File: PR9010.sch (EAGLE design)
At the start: 49 parts, among them U1 SI4703, U2 Tiny85-20-SMT, Y1 32.768kHz

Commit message: Schematics Updates
Recommendations from Andy
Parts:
- removed C15: 1nF, resistor:C-USC0603
- removed L2: 56nH, SparkFun-Passives:INDUCTOR0603
- removed MCU_IO: (no value), SparkFun-Connectors:M06LONGPADS
- removed U$1, U$2: BK-92_MPD_AA_BATT_CLIP, PR_Libraries:BK-92_MPD_AA_BATT_CLIP
- added C10, C13, C8: (no value), SparkFun-Capacitors:1.0UF-25V-+80/-20(0805)
- added J1: AVR_SPI_PRG_6NS, SparkFun-Connectors:AVR_SPI_PRG_6NS
- added L1: (no value), SparkFun-Passives:INDUCTOR0805
- added LED1: (no value), led:LEDSML0603
- added PWRIN, U1AOUT: M02PTH3, SparkFun-Connectors:M02PTH3
- C1: value 0.1uF -> (none); device SparkFun:CAP0402-CAP -> SparkFun-Capacitors:1.0UF-25V-+80/-20(0805)
- C2: value 22nF -> (none); device SparkFun:CAP0402-CAP -> SparkFun-Capacitors:1.0UF-25V-+80/-20(0805)
- C27: value 470pF -> (none)
- C6: value 2.2uF -> (none); device SparkFun:CAP0402-CAP -> SparkFun-Capacitors:1.0UF-25V-+80/-20(0805)
- R5: value 1k -> 1K; device SparkFun:RESISTOR0402-RES -> resistor:R-US_R0603
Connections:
- removed net N$29: C15.2, L2.1, U1.FMIP
- removed net N$30: U$1.NEG, U$2.POS
- removed net N$32: U$1.POS, U$5.SW_OUT
- new net N$10: C1.1, C13.1, C2.1, C6.1, L3.2
- new net N$6: C10.2, L1.1, U1.FMIP
- new net N$7: LED1.A, R5.1
- net 3.3V: now also U$5.SW_OUT; no longer C1.1, C2.1, L3.2, U1.VA, U1.VD, U1.VIO
- net A_IN: no longer C6.2
- net GND: now also C13.2, C6.2, C8.2, J1.6, L1.2, LED1.C, PWRIN.2; no longer L2.2, R19.1, U$2.NEG
- net N$18: now also R15.2
- net N$19: now also C10.1, C8.1; no longer C15.1
- net N$35: now also R19.1; no longer R19.2
- net N$9: now also U1.VA, U1.VD, U1.VIO; no longer R5.2, ST_CH.P1
- net OUT+: no longer AMP.OUT+
- net PB0: now also J1.4; no longer MCU_IO.6
- net PB1: now also J1.1; no longer MCU_IO.5
- net PB2: now also J1.3; no longer MCU_IO.4
- net PB3: now also ST_CH.P1, U1AOUT.1; no longer MCU_IO.3, R5.1
- net PB4: now also R5.2, U1AOUT.2; no longer MCU_IO.2
- net PB5: now also J1.5; no longer MCU_IO.1
- net ROUT: no longer C6.1, U1.ROUT
- net VCC: now also J1.2; no longer R15.2
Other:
- moved on the sheet: C1, C12, C2, C27, C5, C6, C7, ESD, L3, R1, R19, R5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

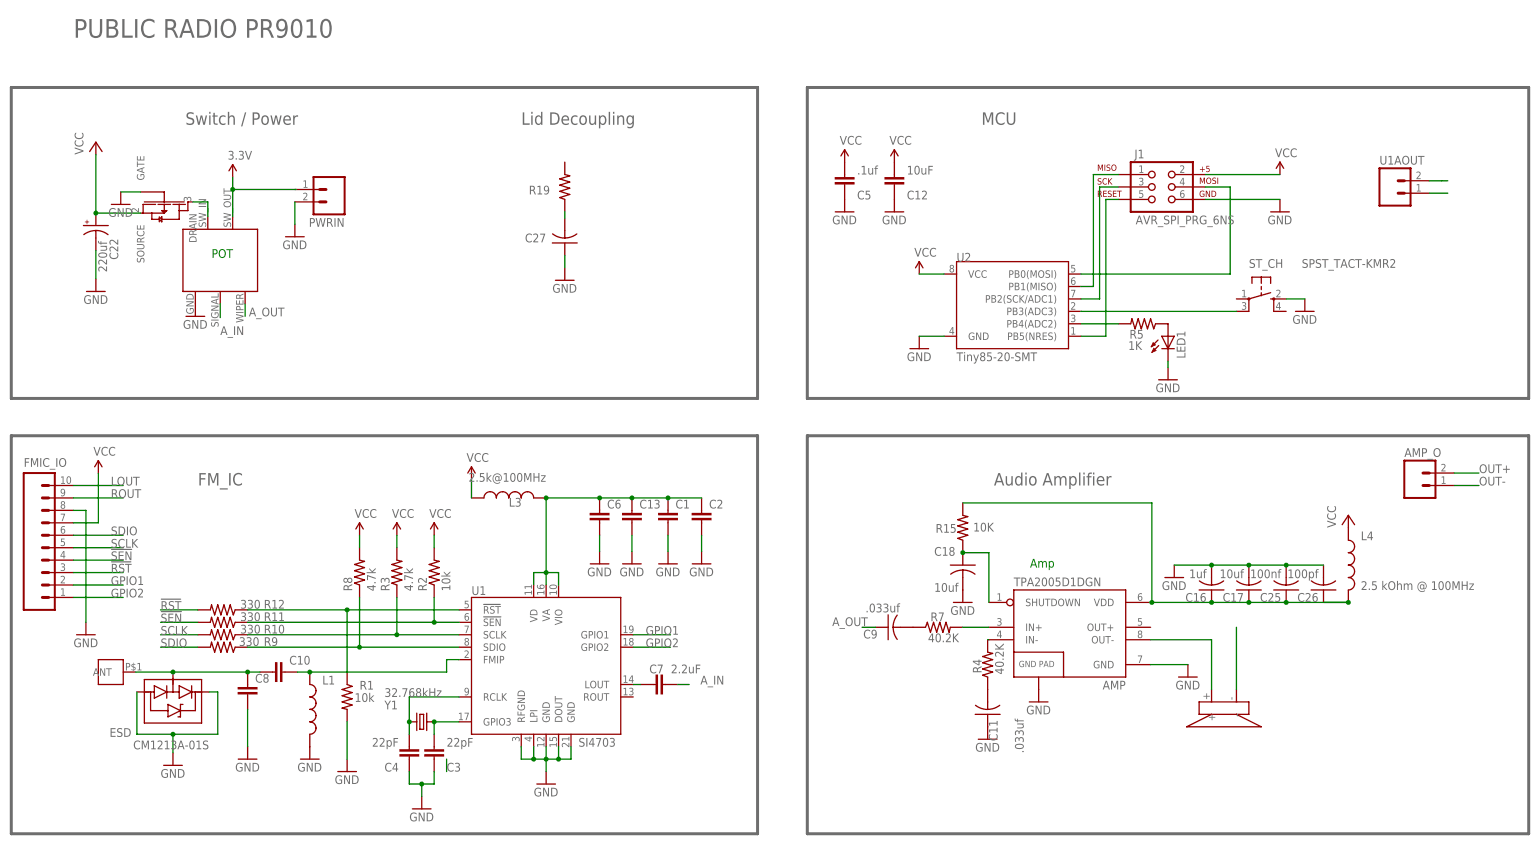
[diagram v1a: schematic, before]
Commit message: Sch Updates
Updates from Andy’s recommendations
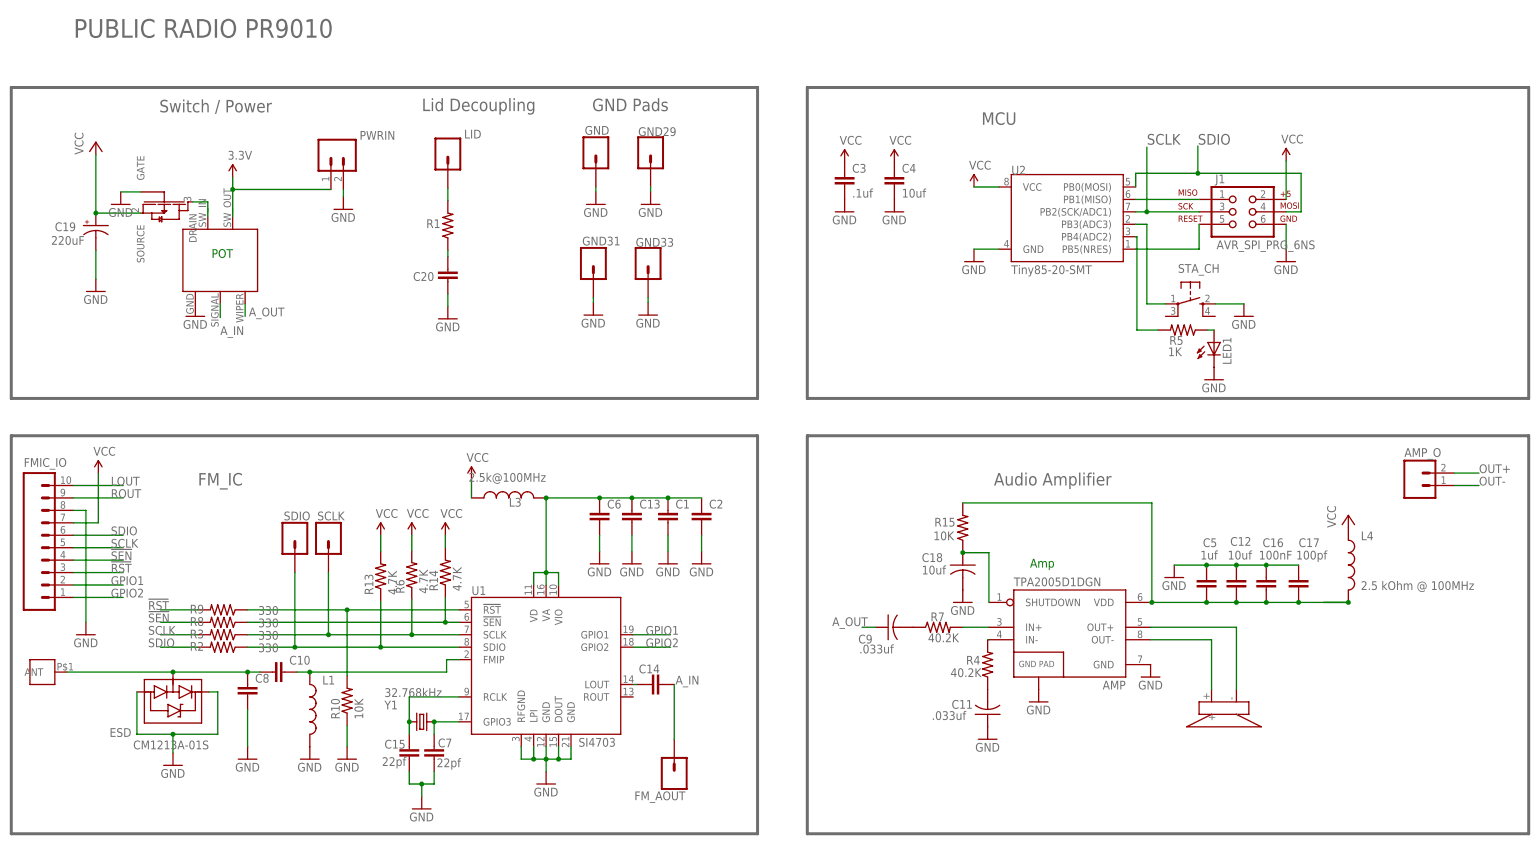
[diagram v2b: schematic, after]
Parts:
- removed C22: 220uf, CPOL-US-LongPads :CPOL-USE2-5
- removed C25: 100nf, resistor:C-USC0603
- removed C26: 100pf, resistor:C-USC0603
- removed C27: (no value), resistor:C-USC0603
- removed R11, R12: 330, SparkFun:RESISTOR0402-RES
- removed R19: 0Ohm, resistor:R-US_R0603
- removed ST_CH: SPST_TACT-KMR2, adafruit:SPST_TACT-KMR2
- removed U1AOUT: M02PTH3, SparkFun-Connectors:M02PTH3
- added C14: 4.7uF, SparkFun-Capacitors:1.0UF-25V-+80/-20(0805)
- added C15: 22pf, SparkFun-Passives:CAP0805
- added C19: 220uF, SparkFun-Passives:CAP_POLC
- added C20: (no value), SparkFun-Passives:CAP0805
- added FM_AOUT, GND, GND29, GND31, GND33, LID, SCLK, SDIO: M01PTH, SparkFun-Connectors:M01PTH
- added R13, R14, R6: 4.7K, SparkFun-Passives:RESISTOR0805-RES
- added STA_CH: SPST_TACT-KMR2, adafruit:SPST_TACT-KMR2
- C12: value 10uF -> 10uf; device SparkFun:CAP0402-CAP -> SparkFun-Passives:CAP0805
- C16: value 1uf -> 100nF; device resistor:C-USC0603 -> SparkFun-Passives:CAP0805
- C17: value 10uf -> 100pf; device resistor:C-USC0603 -> SparkFun-Passives:CAP0805
- C3: value 22pF -> .1uf; device SparkFun:CAP0402-CAP -> SparkFun-Passives:CAP0805
- C4: value 22pF -> 10uf; device SparkFun:CAP0402-CAP -> SparkFun-Passives:CAP0805
- C5: value .1uf -> 1uf; device SparkFun:CAP0402-CAP -> SparkFun-Passives:CAP0805
- C7: value 2.2uF -> 22pf; device SparkFun:CAP0402-CAP -> SparkFun-Passives:CAP0805
- R1: value 10k -> (none); device SparkFun:RESISTOR0402-RES -> SparkFun-Passives:RESISTOR0805-RES
- R10: value 330 -> 10K; device SparkFun:RESISTOR0402-RES -> SparkFun-Passives:RESISTOR0805-RES
- R2: value 10k -> 330; device SparkFun:RESISTOR0402-RES -> SparkFun-Passives:RESISTOR0805-RES
- R3, R8: value 4.7k -> 330; device SparkFun:RESISTOR0402-RES -> SparkFun-Passives:RESISTOR0805-RES
- R9: device SparkFun:RESISTOR0402-RES -> SparkFun-Passives:RESISTOR0805-RES
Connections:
- removed net PB0: J1.4, U2.PB0(MOSI)
- removed net PB2: J1.3, U2.PB2(SCK/ADC1)
- removed net PB3: ST_CH.P1, U1AOUT.1, U2.PB3(ADC3)
- removed net PB4: R5.2, U1AOUT.2, U2.PB4(ADC2)
- new net N$11: STA_CH.P, U2.PB3(ADC3)
- new net N$12: R5.2, U2.PB4(ADC2)
- new net N$8: LID.1, R1.2
- net !RST: now also R9.2; no longer R12.2
- net !RST-L: now also R10.2, R9.1; no longer R1.1, R12.1
- net !SEN: now also R8.2; no longer R11.2
- net !SEN-L: now also R14.1, R8.1; no longer R11.1, R2.1
- net 3.3V: now also PWRIN.1, R13.2, R14.2, R6.2; no longer R2.2, R3.2, R8.2
- net A_IN: now also C14.2, FM_AOUT.1; no longer C7.2
- net GND: now also C15.2, C16.1, C17.1, C19.-, C20.2, C3.2, C4.2, C7.2, GND.1, GND29.1, GND31.1, GND33.1, R10.1, STA_CH.S; no longer C16.2, C17.2, C22.-, C25.2, C26.2, C27.1, C3.1, C4.1, R1.2, ST_CH.S
- net LOUT: now also C14.1; no longer C7.1
- net N$1: now also C15.1; no longer C4.2
- net N$18: now also C12.2, C16.2, C17.2, C5.2; no longer C16.1, C17.1, C25.1, C26.1
- net N$2: now also C7.1; no longer C3.2
- net N$35: now also C20.1, R1.1; no longer C27.2, R19.1
- net OUT+: now also AMP.OUT+
- net SCLK: now also J1.3, R3.2, U2.PB2(SCK/ADC1); no longer R10.2
- net SCLK-L: now also R6.1, SCLK.1; no longer R10.1
- net SDIO: now also J1.4, R2.2, U2.PB0(MOSI); no longer R9.2
- net SDIO-L: now also R13.1, R2.1, SDIO.1; no longer R8.1, R9.1
- net VCC: now also C19.+, C3.1, C4.1; no longer C12.2, C22.+, C5.2
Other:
- note added: "GND Pads"
- moved on the sheet: C12, C16, C17, C3, C4, C5, C7, J1, LED1, PWRIN, R1, R10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

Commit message: Sch Updates
Updates based on Andy’s recommendations.
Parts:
- removed SCLK, SDIO: M01PTH, SparkFun-Connectors:M01PTH
- removed U$3: CE32A_DAYTON_SPKR, PR_Libraries:CE32A_DAYTON_SPKR
- added SCLK_BUS, SDIO_BUS: M01PTH, SparkFun-Connectors:M01PTH
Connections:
- net OUT+: now also AMP_O.1; no longer AMP_O.2, U$3.-
- net OUT-: now also AMP_O.2; no longer AMP_O.1, U$3.+
- net SCLK-L: now also SCLK_BUS.1; no longer SCLK.1
- net SDIO-L: now also SDIO_BUS.1; no longer SDIO.1
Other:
- moved on the sheet: AMP_O
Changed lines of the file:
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@@
 <part name="GND23" library="SparkFun-Aesthetics" deviceset="GND" device=""/>
 <part name="ESD" library="PubRadioLib" deviceset="CM1213A-01S" device=""/>
-<part name="U$3" library="PR_Libraries" deviceset="CE32A_DAYTON_SPKR" device=""/>
 <part name="FET" library="PubRadioLib" deviceset="SI2333DDS" device=""/>
 <part name="GND24" library="SparkFun-Aesthetics" deviceset="GND" device=""/>
@@
 <part name="FM_AOUT" library="SparkFun-Connectors" deviceset="M01" device="PTH"/>
 <part name="C19" library="SparkFun-Passives" deviceset="CAP_POL" device="C" value="220uF"/>
-<part name="SDIO" library="SparkFun-Connectors" deviceset="M01" device="PTH"/>
-<part name="SCLK" library="SparkFun-Connectors" deviceset="M01" device="PTH"/>
+<part name="SDIO_BUS" library="SparkFun-Connectors" deviceset="M01" device="PTH"/>
+<part name="SCLK_BUS" library="SparkFun-Connectors" deviceset="M01" device="PTH"/>
 <part name="C20" library="SparkFun-Passives" deviceset="CAP" device="0805"/>
 <part name="R1" library="SparkFun-Passives" deviceset="RESISTOR" device="0805-RES"/>
@@
 <attribute name="VALUE" x="-15.748" y="17.2466" size="1.778" layer="96"/>
 </instance>
-<instance part="U$3" gate="G$1" x="207.01" y="26.924" rot="MR270"/>
 <instance part="FET" gate="G$1" x="-9.398" y="128.524" rot="R270"/>
 <instance part="GND24" gate="1" x="-18.288" y="128.524"/>
@@
 </instance>
 <instance part="GND13" gate="1" x="211.074" y="105.664"/>
-<instance part="AMP_O" gate="G$1" x="246.38" y="71.12" smashed="yes">
-<attribute name="NAME" x="243.84" y="76.962" size="1.778" layer="95"/>
+<instance part="AMP_O" gate="G$1" x="230.886" y="42.164" smashed="yes" rot="R180">
+<attribute name="NAME" x="233.426" y="36.322" size="1.778" layer="95" rot="R180"/>
 </instance>
 <instance part="J1" gate="G$1" x="209.55" y="127"/>
@@
 <attribute name="VALUE" x="-32.512" y="120.269" size="1.778" layer="96"/>
 </instance>
-<instance part="SDIO" gate="G$1" x="17.272" y="60.96" smashed="yes" rot="R270">
-<attribute name="NAME" x="14.986" y="64.008" size="1.778" layer="95"/>
-</instance>
-<instance part="SCLK" gate="G$1" x="24.13" y="60.96" smashed="yes" rot="R270">
-<attribute name="NAME" x="21.844" y="64.008" size="1.778" layer="95"/>
+<instance part="SDIO_BUS" gate="G$1" x="15.748" y="60.96" smashed="yes" rot="R270">
+<attribute name="NAME" x="5.588" y="63.754" size="1.778" layer="95"/>
+</instance>
+<instance part="SCLK_BUS" gate="G$1" x="22.86" y="60.96" smashed="yes" rot="R270">
+<attribute name="NAME" x="19.812" y="64.008" size="1.778" layer="95"/>
 </instance>
 <instance part="C20" gate="G$1" x="48.514" y="112.776" smashed="yes">
@@
 <wire x1="50.8" y1="40.64" x2="41.148" y2="40.64" width="0.1524" layer="91"/>
 <wire x1="41.148" y1="47.752" x2="41.148" y2="40.64" width="0.1524" layer="91"/>
-<wire x1="41.148" y1="40.64" x2="24.13" y2="40.64" width="0.1524" layer="91"/>
+<wire x1="41.148" y1="40.64" x2="22.86" y2="40.64" width="0.1524" layer="91"/>
 <junction x="41.148" y="40.64"/>
 <pinref part="U1" gate="G$1" pin="SCLK"/>
 <pinref part="R6" gate="G$1" pin="1"/>
 <pinref part="R3" gate="G$1" pin="1"/>
-<wire x1="24.13" y1="40.64" x2="7.62" y2="40.64" width="0.1524" layer="91"/>
-<junction x="24.13" y="40.64"/>
-<pinref part="SCLK" gate="G$1" pin="1"/>
-<wire x1="24.13" y1="53.34" x2="24.13" y2="40.64" width="0.1524" layer="91"/>
+<wire x1="22.86" y1="40.64" x2="7.62" y2="40.64" width="0.1524" layer="91"/>
+<junction x="22.86" y="40.64"/>
+<pinref part="SCLK_BUS" gate="G$1" pin="1"/>
+<wire x1="22.86" y1="53.34" x2="22.86" y2="40.64" width="0.1524" layer="91"/>
 </segment>
 </net>
@@
 <wire x1="50.8" y1="38.1" x2="34.798" y2="38.1" width="0.1524" layer="91"/>
 <wire x1="34.798" y1="47.498" x2="34.798" y2="38.1" width="0.1524" layer="91"/>
-<wire x1="34.798" y1="38.1" x2="17.272" y2="38.1" width="0.1524" layer="91"/>
+<wire x1="34.798" y1="38.1" x2="15.748" y2="38.1" width="0.1524" layer="91"/>
 <junction x="34.798" y="38.1"/>
 <pinref part="U1" gate="G$1" pin="SDIO"/>
 <pinref part="R13" gate="G$1" pin="1"/>
 <pinref part="R2" gate="G$1" pin="1"/>
-<wire x1="17.272" y1="38.1" x2="7.62" y2="38.1" width="0.1524" layer="91"/>
-<junction x="17.272" y="38.1"/>
-<pinref part="SDIO" gate="G$1" pin="1"/>
-<wire x1="17.272" y1="53.34" x2="17.272" y2="38.1" width="0.1524" layer="91"/>
+<wire x1="15.748" y1="38.1" x2="7.62" y2="38.1" width="0.1524" layer="91"/>
+<junction x="15.748" y="38.1"/>
+<pinref part="SDIO_BUS" gate="G$1" pin="1"/>
+<wire x1="15.748" y1="53.34" x2="15.748" y2="38.1" width="0.1524" layer="91"/>
 </segment>
 </net>
@@
 <net name="OUT-" class="0">
 <segment>
-<pinref part="U$3" gate="G$1" pin="+"/>
-<wire x1="204.47" y1="29.464" x2="204.47" y2="39.624" width="0.1524" layer="91"/>
 <pinref part="AMP" gate="G$1" pin="OUT-"/>
-<wire x1="192.024" y1="39.624" x2="204.47" y2="39.624" width="0.1524" layer="91"/>
-</segment>
-<segment>
+<wire x1="192.024" y1="39.624" x2="223.266" y2="39.624" width="0.1524" layer="91"/>
+<pinref part="AMP_O" gate="G$1" pin="2"/>
+<label x="224.028" y="39.116" size="2.1844" layer="95" rot="R180"/>
+</segment>
+</net>
+<net name="OUT+" class="0">
+<segment>
+<pinref part="AMP" gate="G$1" pin="OUT+"/>
+<wire x1="192.024" y1="42.164" x2="223.266" y2="42.164" width="0.1524" layer="91"/>
 <pinref part="AMP_O" gate="G$1" pin="1"/>
-<wire x1="254" y1="71.12" x2="259.08" y2="71.12" width="0.1524" layer="91"/>
-<label x="259.08" y="71.12" size="1.778" layer="95"/>
-</segment>
-</net>
-<net name="OUT+" class="0">
-<segment>
-<pinref part="U$3" gate="G$1" pin="-"/>
-<wire x1="209.55" y1="29.464" x2="209.55" y2="42.164" width="0.1524" layer="91"/>
-<pinref part="AMP" gate="G$1" pin="OUT+"/>
-<wire x1="192.024" y1="42.164" x2="209.55" y2="42.164" width="0.1524" layer="91"/>
-</segment>
-<segment>
-<pinref part="AMP_O" gate="G$1" pin="2"/>
-<wire x1="254" y1="73.66" x2="259.08" y2="73.66" width="0.1524" layer="91"/>
-<label x="259.08" y="73.66" size="1.778" layer="95"/>
-</segment>
-</net>
+<label x="224.028" y="44.45" size="2.1844" layer="95" rot="R180"/>
+</segment>
+</net>

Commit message: Sch Updates
Continuing to update the PR9010 sch
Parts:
- removed ESD: CM1213A-01S, PubRadioLib:CM1213A-01S
- added D1: (no value), SparkFun-DiscreteSemi:BAV99
- added U$1, U$2: BK-92_MPD_AA_BATT_CLIP, PR_Libraries:BK-92_MPD_AA_BATT_CLIP
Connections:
- removed net N$10: C1.1, C13.1, C2.1, C6.1, L3.2
- removed net N$19: ANT.ANT, C10.1, C8.1, ESD.CH
- new net N$13: U$1.NEG, U$2.POS
- new net N$14: ANT.ANT, D1.A1
- new net N$15: PWRIN.1, U$1.POS, U$5.SW_OUT
- new net N$17: C10.1, C8.1, D1.C2
- net 3.3V: no longer PWRIN.1, U$5.SW_OUT
- net GND: now also D1.COM, U$2.NEG; no longer ESD.VN, ESD.VP
- net N$9: now also C1.1, C13.1, C2.1, C6.1, L3.2
